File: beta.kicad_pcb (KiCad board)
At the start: 2 copper layers, 72 x 54.6 mm, 11 parts, among them J1 PSX Memory Card Interface, J2 MicroSD SPI, U1 RP2040-ZERO, U4 psram

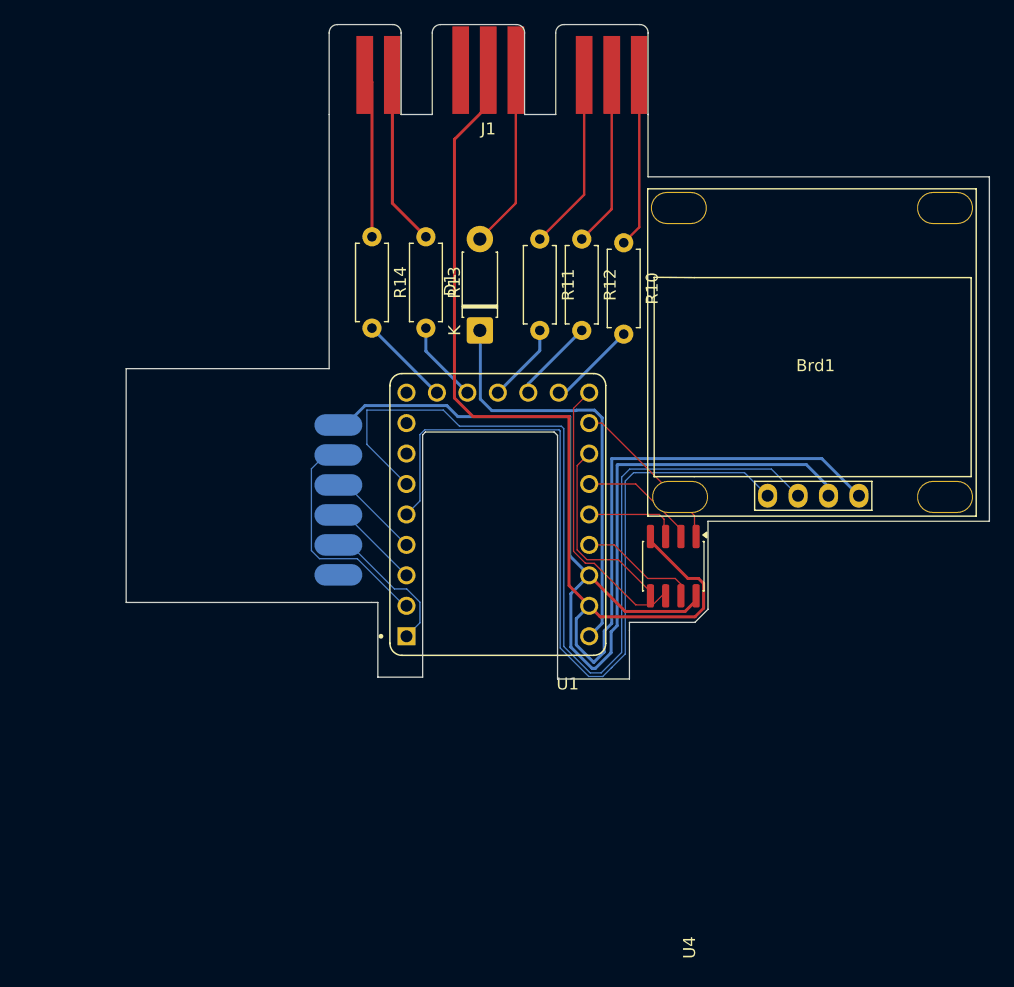
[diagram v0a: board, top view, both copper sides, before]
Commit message: Add files via upload
changes the pcb to be more compacted, added the tactile buttons and made the layers gnd and 3.3v
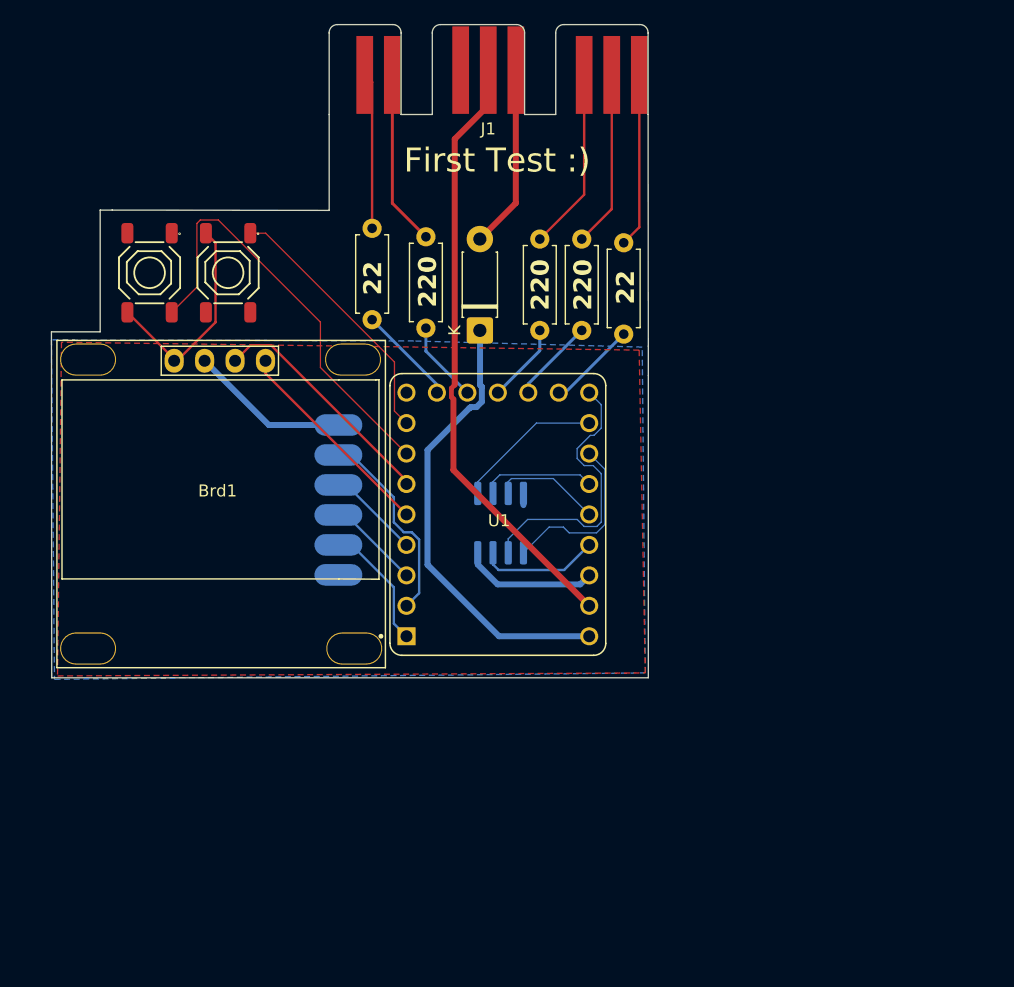
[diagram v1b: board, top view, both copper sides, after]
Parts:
- added S1: Tactile Button, 160gf, PCM_JLCPCB:SW-SMD_4P-L5.1-W5.1-P3.70-LS6.5-TL-2, F.Cu at (47.5, 70.0)
- added S2: Tactile Button, 160gf, PCM_JLCPCB:SW-SMD_4P-L5.1-W5.1-P3.70-LS6.5-TL-2, F.Cu at (41.0, 70.0)
- U4: moved to B.Cu
- moved Brd1 50.9 mm to (46.6, 87.9), turned to 0 degrees
- moved U4 14.8 mm to (70.2, 90.9)
- moved R14 0.71 mm to (59.5, 66.3)
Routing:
- net +3V3: track 91.6 -> 24.6 mm
- net OLED_SCL: track 79.7 -> 19.8 mm
- net OLED_SDA: track 71.7 -> 17.7 mm
- net GND: track 121.6 -> 69.9 mm
- net SW3: track 0.00 -> 36.2 mm
- net SW2: track 0.00 -> 22.0 mm
- net SS: track 19.4 -> 16.8 mm
- net Net-(D1-K): track 35.3 -> 37.7 mm
- net PSRAM_IO2: track 7.38 -> 9.08 mm
- net MISO: track 12.1 -> 10.6 mm
- net PSRAM_IO0: track 15.8 -> 14.6 mm
- net PSRAM_CS: track 13.2 -> 12.3 mm
- net Net-(U1-GP9): track 7.65 -> 8.37 mm
- added copper zone on F.Cu, net +3V3
- added copper zone on B.Cu, net GND
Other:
- board size 72 x 54.6 mm -> 49.8 x 54.5 mm
- board text added: "22"
- board text added: "220"
- board text added: "First Test :)"

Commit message: Add files via upload
Here oled and buttons should be properly visible while plugged in, i am waiting for a part to test if 4677 works and if it does i will order the pcbs to see that would work, please PLEASE dont order any pcbs unless i say other wise for your own benefit
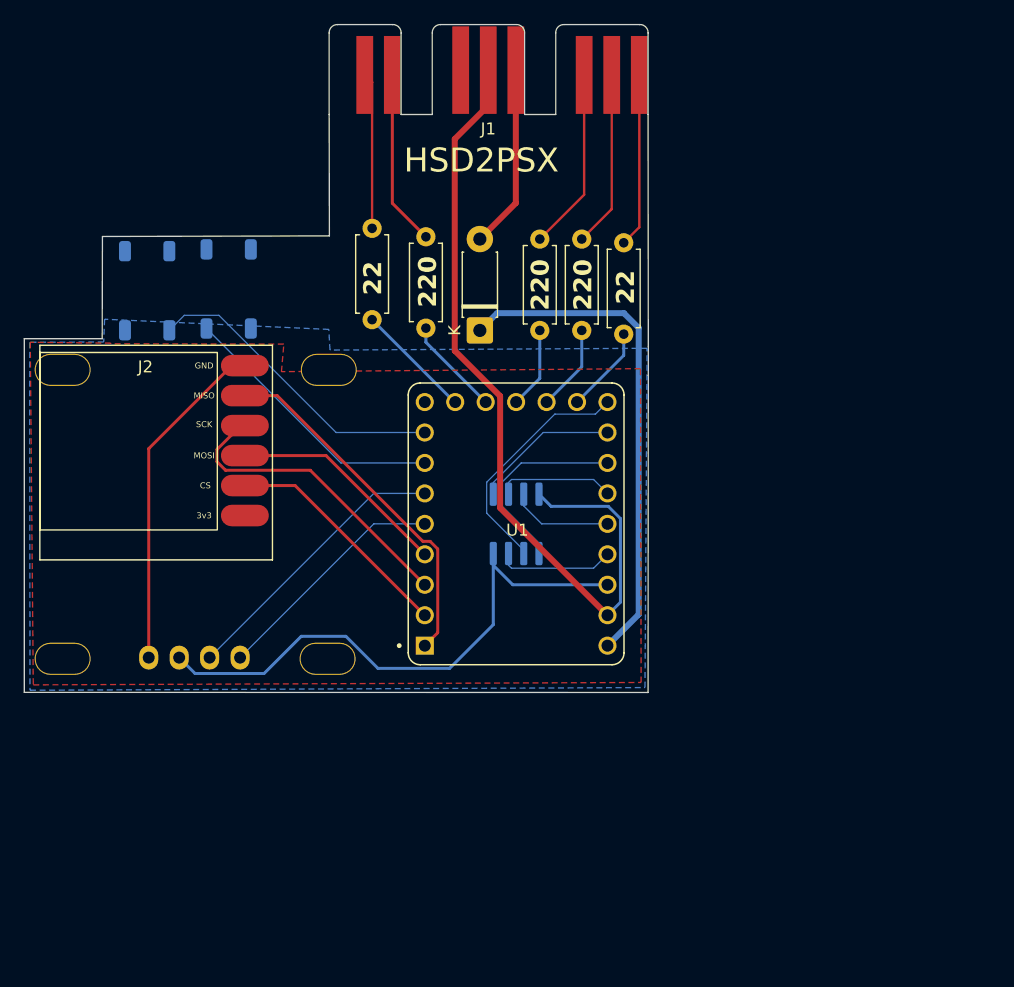
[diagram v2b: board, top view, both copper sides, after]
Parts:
- Brd1, S1, S2: moved to B.Cu
- J2: moved to F.Cu
- moved J2 9.29 mm to (47.7, 84.0)
- moved S1 6.91 mm to (40.8, 71.5), turned to 90 degrees
- moved S2 6.74 mm to (47.5, 71.3)
- moved Brd1 4.14 mm to (44.5, 91.5)
- moved U1 1.72 mm to (71.5, 90.9)
- moved U4 1.30 mm to (71.5, 90.9)
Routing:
- net GND: track 69.9 -> 96.4 mm
- net +3V3: track 24.6 -> 47.8 mm
- net MISO: track 10.6 -> 29.9 mm
- net SCK: track 7.77 -> 25.8 mm
- net SW3: track 36.2 -> 22.9 mm
- net MOSI: track 7.75 -> 18.4 mm
- net Net-(D1-K): track 37.7 -> 42.0 mm
- net SW2: track 22.0 -> 25.9 mm
- net OLED_SCL: track 19.8 -> 23.6 mm
- net PSRAM_CLK: track 23.5 -> 20.1 mm
- net SS: track 16.8 -> 19.5 mm
- net OLED_SDA: track 17.7 -> 20.0 mm
- net PSRAM_IO0: track 14.6 -> 16.7 mm
- net Net-(U1-GP9): track 8.37 -> 9.78 mm
- net Net-(U1-GP10): track 7.39 -> 8.23 mm
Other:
- board size 49.8 x 54.5 mm -> 52 x 55.7 mm
- board text added: "HSD2PSX"
- board text removed: "First Test :)"
